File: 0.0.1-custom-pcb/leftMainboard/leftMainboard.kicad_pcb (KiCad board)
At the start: 2 copper layers, 45 x 75.3 mm, 78 parts, among them J1 USB-C USB2 receptacle (footpr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, J10 HC-FPC-0.5-12P-FH20, J2 3-pin LiPo / NTC 1.25mm (esti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, J3 GPIO / SWD 2x6 1.27mm, J7 HC-FPC-0.5-14P-FH20, J8 HC-FPC-0.5-12P-FH20, J9 HC-FPC-0.5-12P-FH20, Q1 BSS138 (guess), Q2 P-channel MOSFET (guess), Q3 P-channel MOSFET (guess), SW1 Latching DPDT power push swit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, SW2 Reset tactile 4x4mm (estimate), U1 Boost controller MSOP8 (unide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, U2 TP4056-42-ESOP8, U3 PRTR5V0U2X, U4 MDBT50Q-P1MV2, U5 74CBTLV1G125GV (probable b25 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, Y1 32.768kHz (guess)

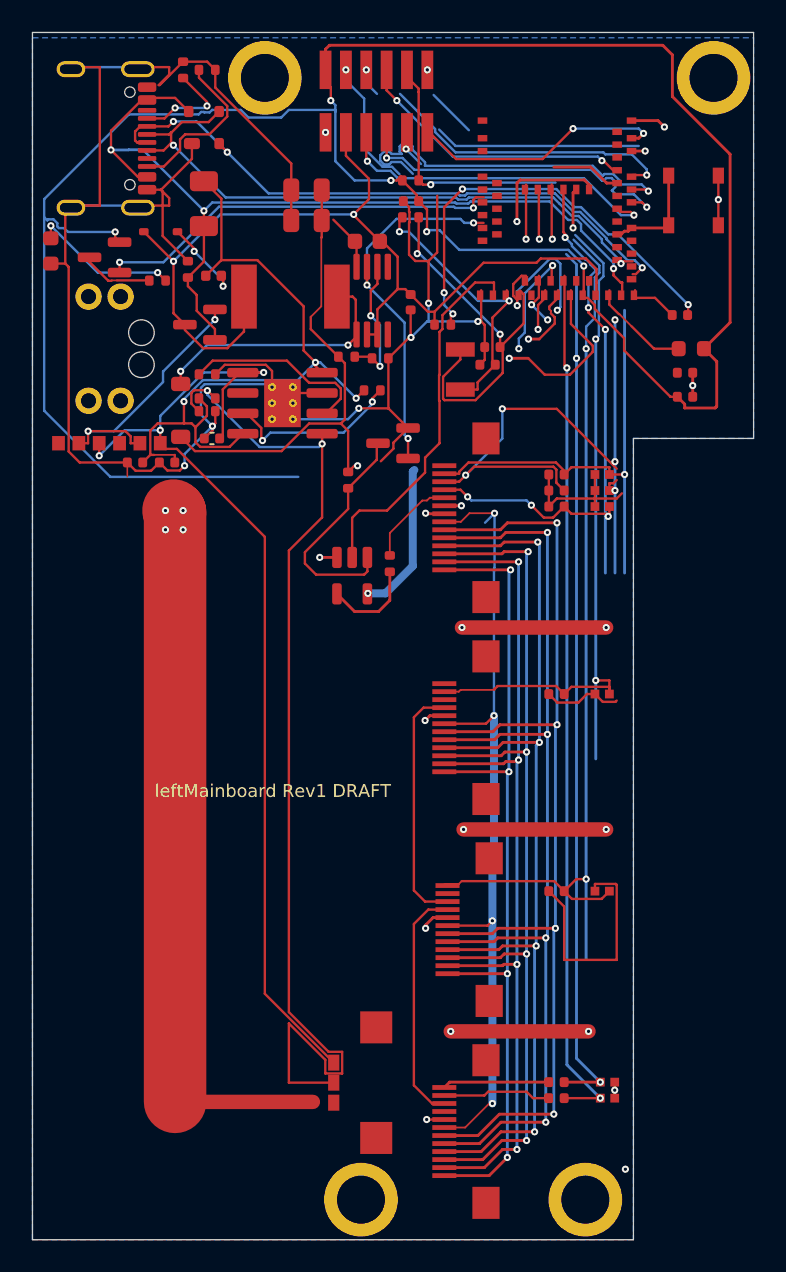
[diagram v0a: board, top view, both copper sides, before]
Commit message: get correct main switch
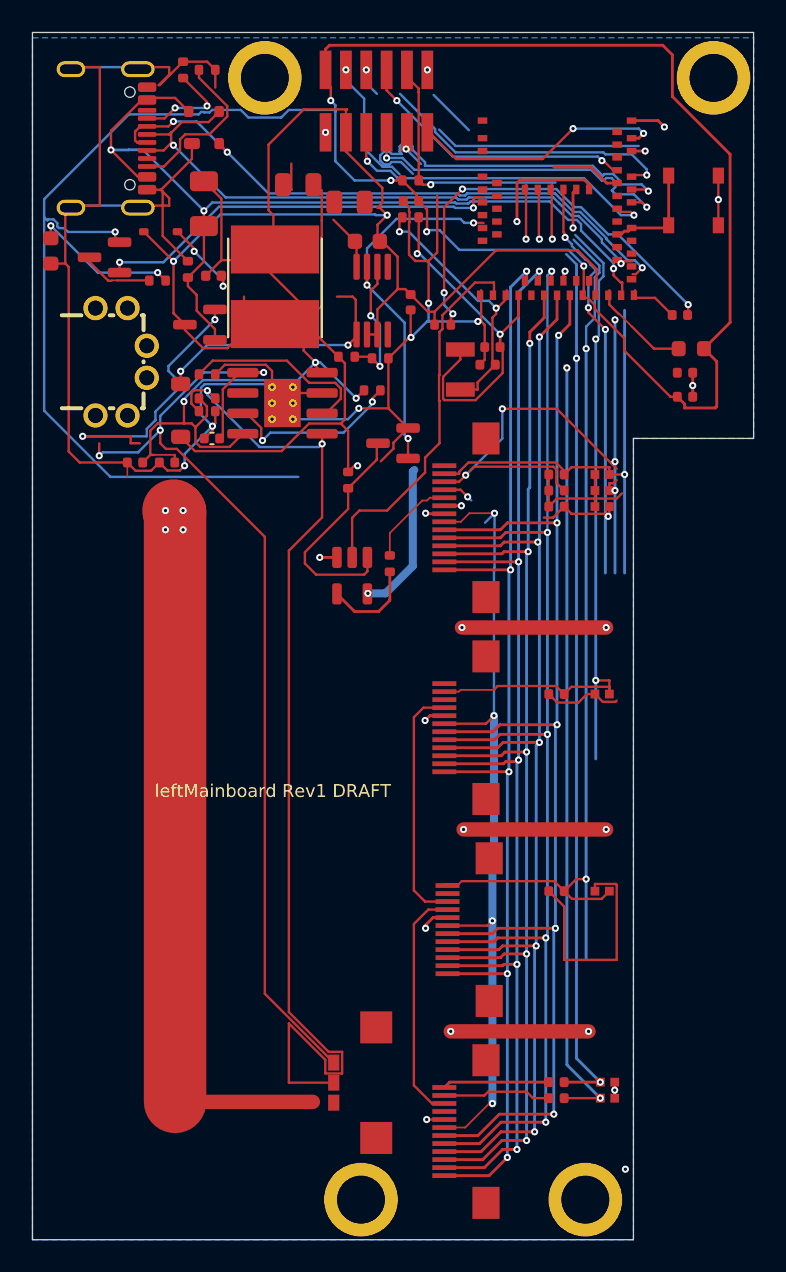
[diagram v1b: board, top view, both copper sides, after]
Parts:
- L1: value 33uH -> 1.8uH; footprint Reconstruction:L1_Inductor_6x6mm_PhotoEstimate -> Reconstruction:L_XRCD54_5.8x5.2mm_C5339378
- SW1: value Latching DPDT power push switch (estimate) -> TK-6580A-1; footprint Reconstruction:PowerSwitch_DPDT_LH_PhotoEstimate -> Reconstruction:SW_TK6580A1_C528770
- moved C20 2.91 mm to (69.7, 60.4)
- moved SW1 1.10 mm to (55.4, 70.3), turned to -90 degrees
- moved L1 0.97 mm to (65.0, 65.7), turned to 90 degrees
- moved C1 0.61 mm to (66.5, 59.3)
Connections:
- SW1 pad 2: VBAT_SWITCHED -> VBAT
- SW1 pad 4: VBAT -> VBAT_SWITCHED
- SW1 pad 5: VBAT_SWITCHED -> unconnected-(SW1-NC_B-Pad5)
- SW1 pad 6: unconnected-(SW1-Pad6) -> VBAT_SWITCHED
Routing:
- net R1: track 58.8 -> 74.8 mm, vias 6 -> 5
- net VDDH: track 59.2 -> 74.7 mm
- net R2: track 60.6 -> 74.4 mm
- net R3: track 65.2 -> 76.6 mm
- net R4: track 69.8 -> 79.8 mm, vias 6 -> 5
- net R0: track 63.0 -> 72.7 mm, vias 6 -> 5
- net GND: track 238.6 -> 230.0 mm
- net C2: track 37.6 -> 32.7 mm, vias 6 -> 5
- net C6: track 61.4 -> 56.5 mm, vias 2 -> 3
- net R5: track 76.3 -> 80.2 mm
- net VBAT_SWITCHED: track 16.9 -> 18.2 mm
- net XL1: track 18.0 -> 17.3 mm
- net XL2: track 24.3 -> 23.7 mm
